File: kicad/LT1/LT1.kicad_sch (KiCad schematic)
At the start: 79 parts, among them J1 USB_B_Micro, J2 Conn_01x05_Socket, J3 Conn_01x02_Socket, J4 Conn_01x02_Socket, Q31 2N7002K, Q32 2N7002K, SW1 SW_Push, SW2 SW_Push, SW3 SW_Push, SW4 SW_Push, SW5 SW_Push, SW6 SW_Push, SW7 SW_Push, U1 MCP73831-2-OT, U2 TLV75533PDBV, U8 MCP111T-xxxE_TT, U9 STM32L412C8Tx, Y1 32 kHz (ABS06)

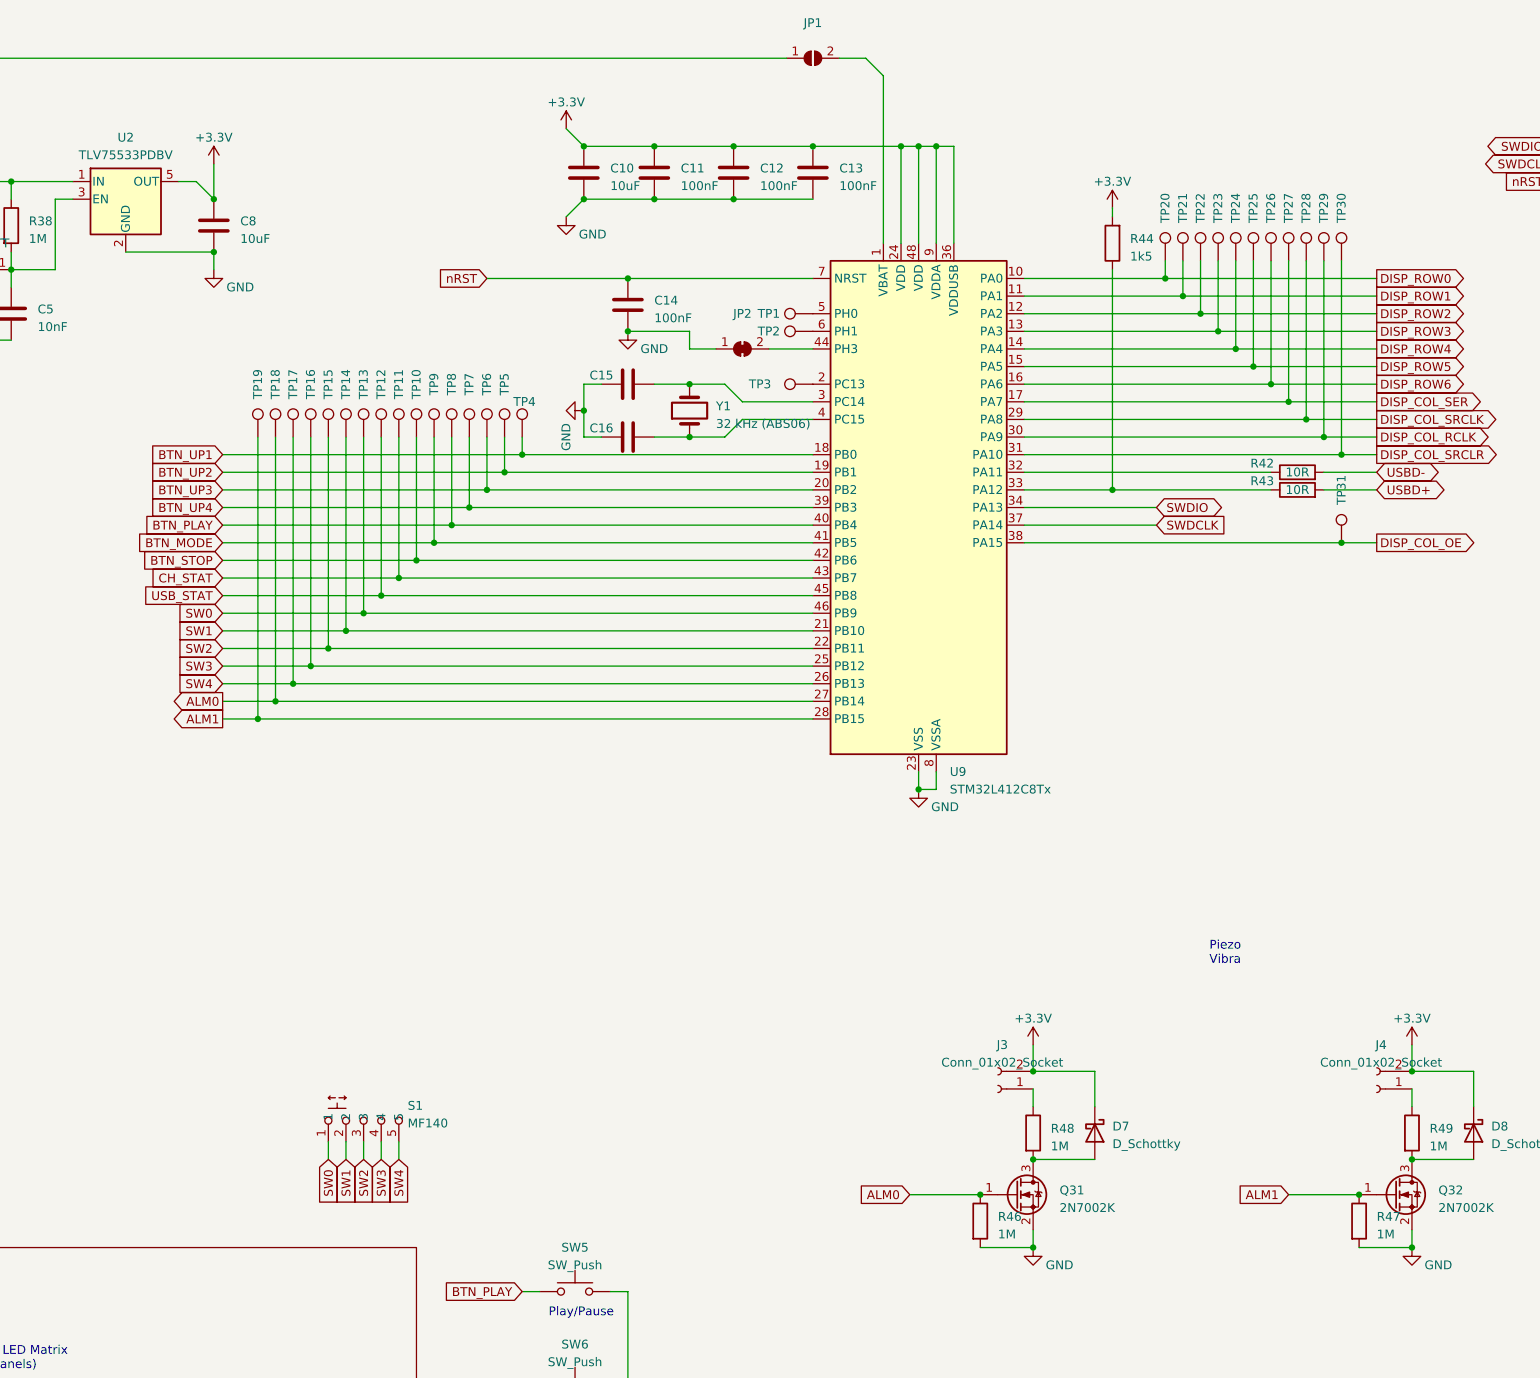
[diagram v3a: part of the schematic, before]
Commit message: LT1 some routing and placing
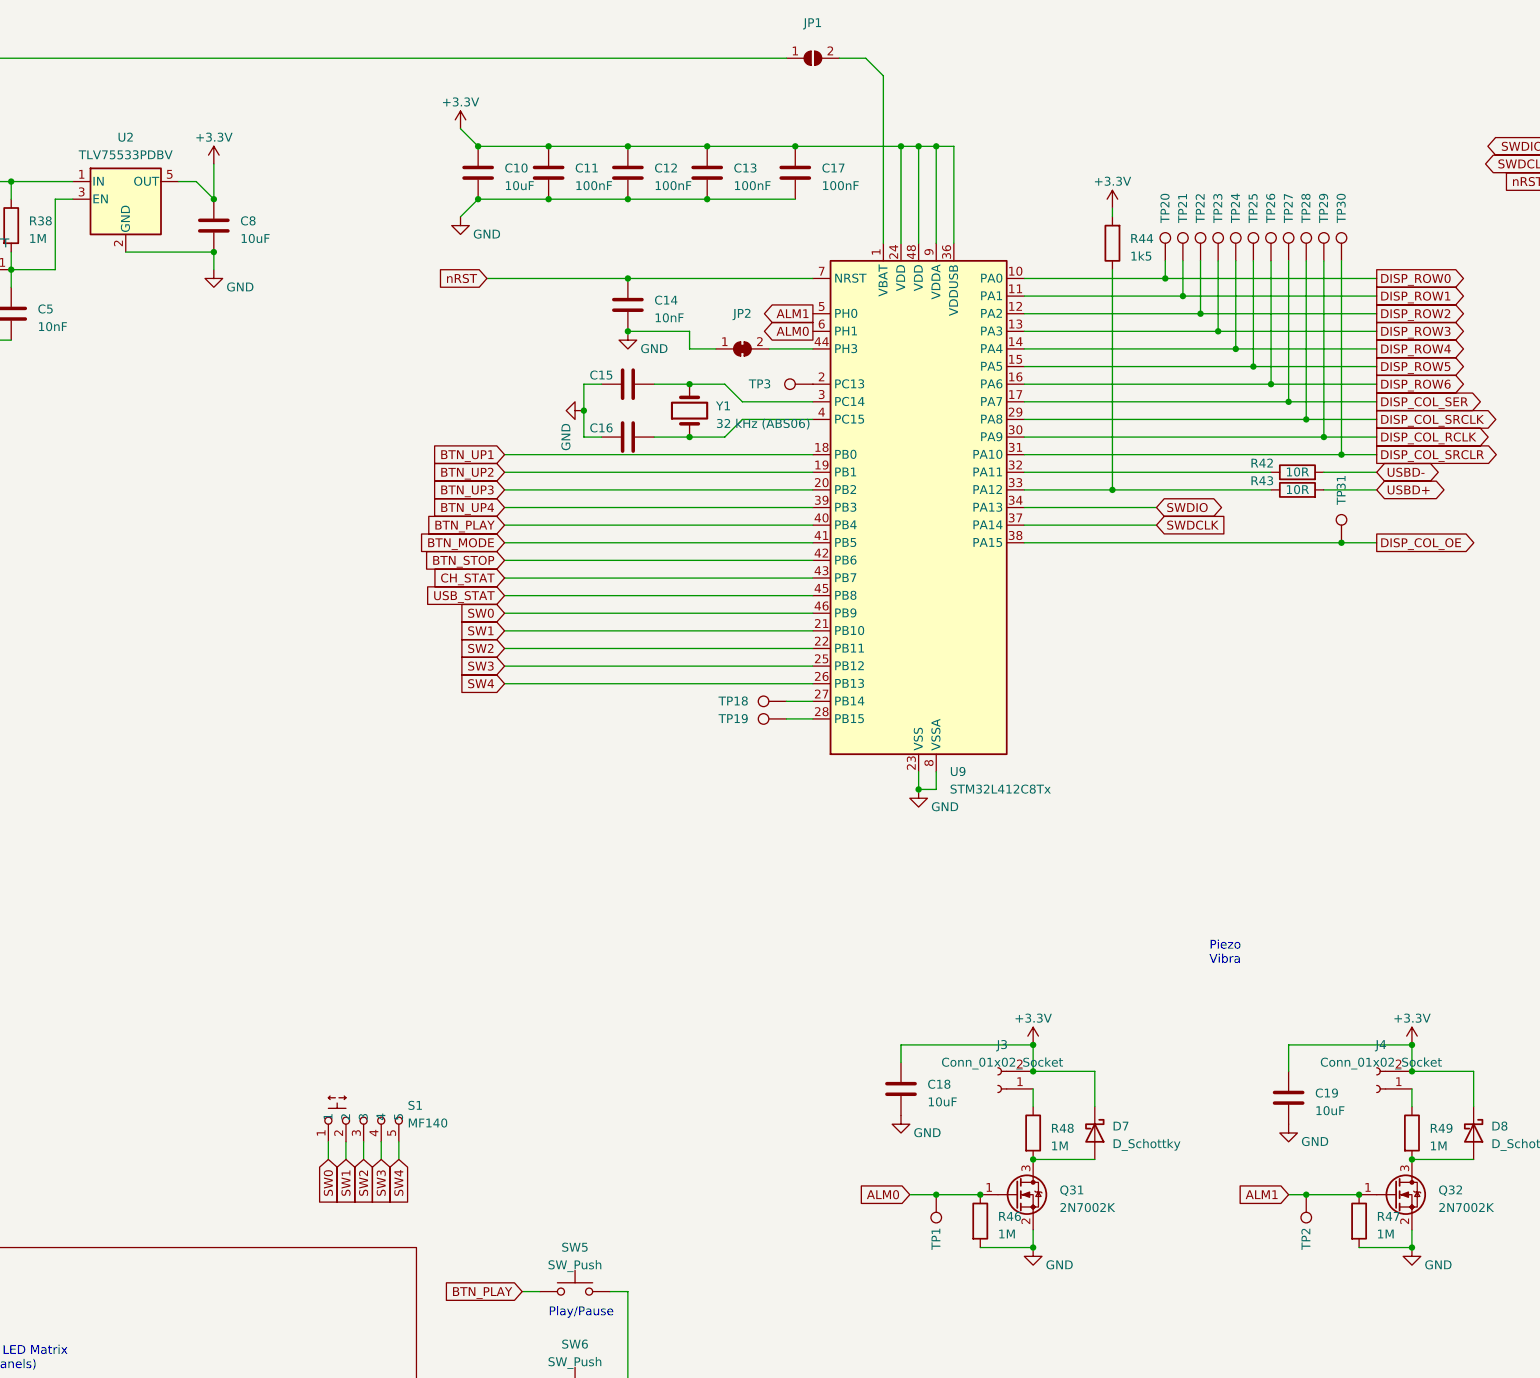
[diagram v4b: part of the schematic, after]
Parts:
- removed TP10, TP11, TP12, TP13, TP14, TP15, TP16, TP17, TP4, TP5, TP6, TP7, TP8, TP9: TestPoint, TestPoint:TestPoint_Pad_D1.0mm, symbol Connector:TestPoint
- added C17: 100nF, Capacitor_SMD:C_0603_1608Metric, symbol Device:C
- added C18, C19: 10uF, Capacitor_SMD:C_0805_2012Metric, symbol Device:C
- C14: value 100nF -> 10nF
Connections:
- net +3.3V: now also C17.1, C18.1, C19.1
- net ALM0: now also TP1.1, U9.6 (PH1); no longer TP18.1, U9.27 (PB14)
- net ALM1: now also TP2.1, U9.5 (PH0); no longer TP19.1, U9.28 (PB15)
- net GND: now also C17.2, C18.2, C19.2
- new net: TP18.1, U9.27 (PB14)
- new net: TP19.1, U9.28 (PB15)
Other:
- moved on the sheet: C10, C11, C12, C13, TP1, TP18, TP19, TP2
